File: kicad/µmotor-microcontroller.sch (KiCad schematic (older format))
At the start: 9 parts, among them J201 TX, J202 RX, J203 SWDIO, J204 SWCLK, J205 GND, U201 STM32F042F6Px

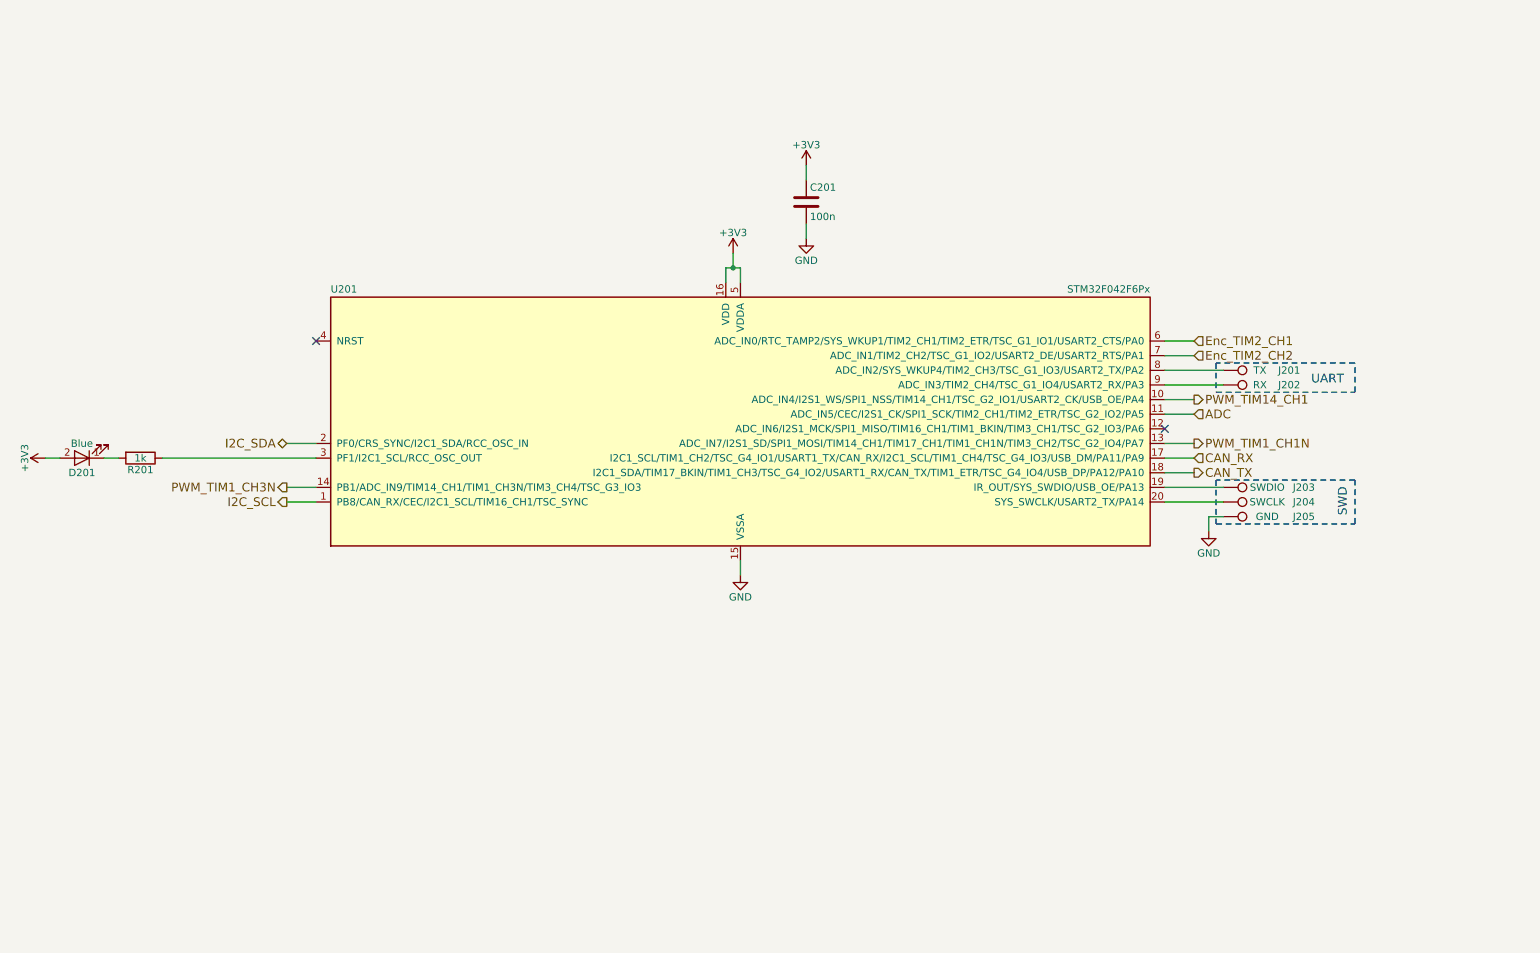
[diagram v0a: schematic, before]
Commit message: second design: STM32L432KC µC with DRV8323S gate driver and FDMD82xx FETs
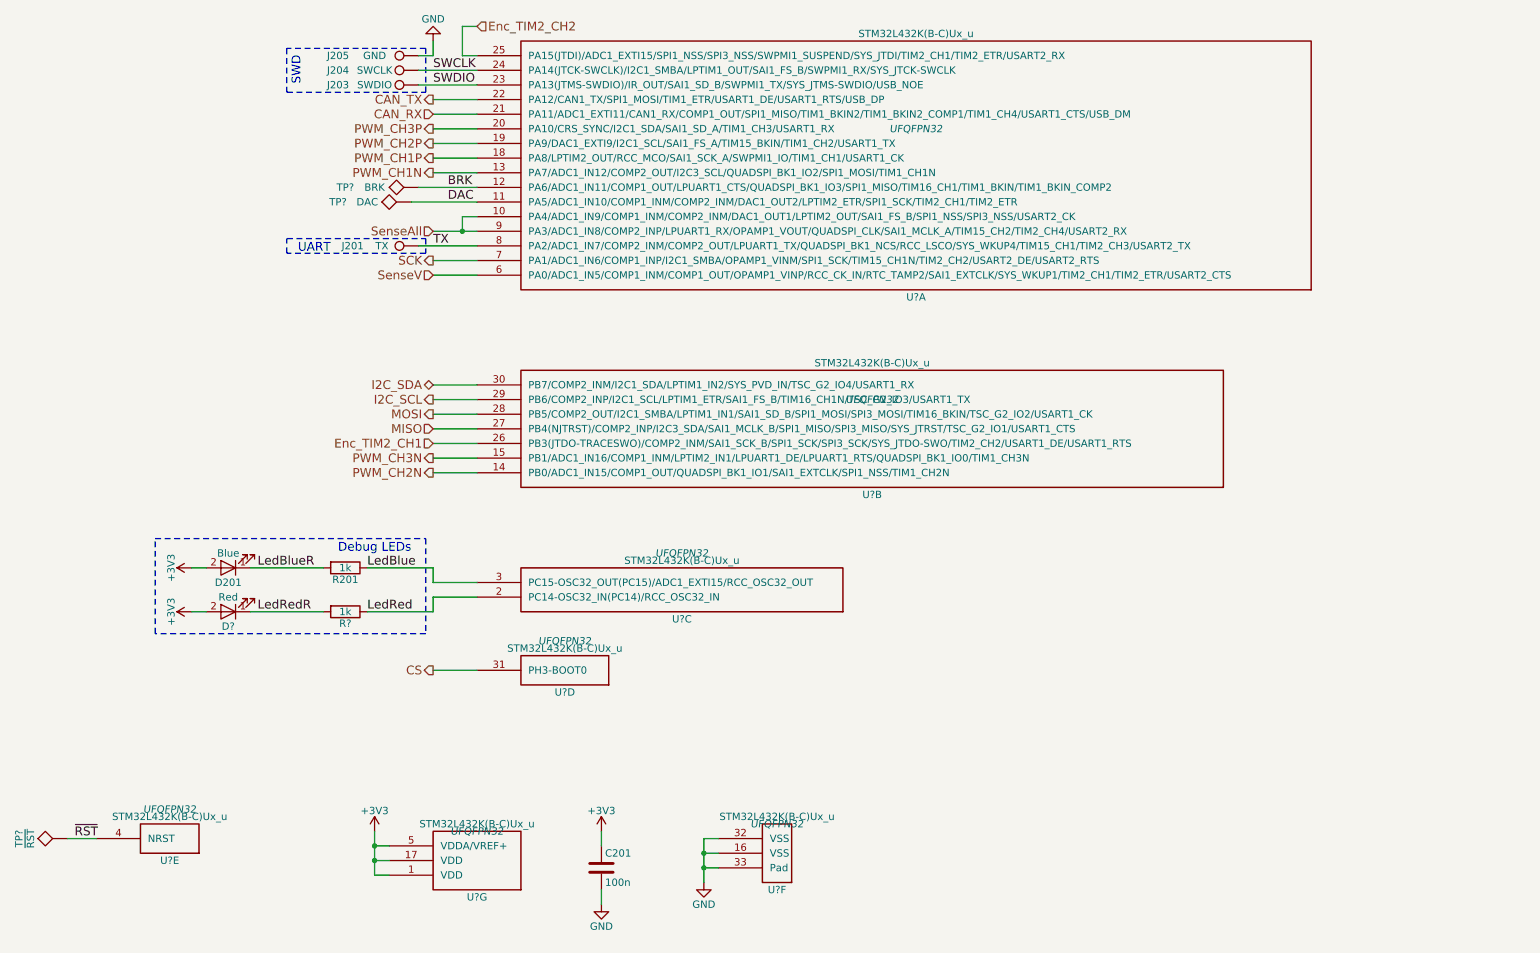
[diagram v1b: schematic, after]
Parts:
- removed J202: RX, Measurement_Points:Measurement_Point_Round-SMD-Pad_Small, symbol TEST_1P
- removed U201: STM32F042F6Px, Housings_SSOP:TSSOP-20_4.4x6.5mm_Pitch0.65mm, symbol STM32F042F6Px
- added D?: Red, LEDs:LED_0603, symbol LED
- added R?: 1k, Resistors_SMD:R_0603, symbol R
- added TP?: ~RST, symbol TEST
- added TP?: BRK, symbol TEST
- added TP?: DAC, symbol TEST
- added U? (x7): STM32L432K(B-C)Ux_u, UFQFPN32, symbol STM32L432K(B-C)Ux_u
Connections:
- net +3V3: now also D?.2 (A), U?.1 (VDD), U?.17 (VDD), U?.5 (VDDA/VREF+)
- net CAN_RX: now also U?.21 (PA11/ADC1_EXTI11/CAN1_RX/COMP1_OUT/SPI1_MISO/TIM1_BKIN2/TIM1_BKIN2_COMP1/TIM1_CH4/USART1_CTS/USB_DM)
- net CAN_TX: now also U?.22 (PA12/CAN1_TX/SPI1_MOSI/TIM1_ETR/USART1_DE/USART1_RTS/USB_DP)
- net Enc_TIM2_CH1: now also U?.26 (PB3(JTDO-TRACESWO)/COMP2_INM/SAI1_SCK_B/SPI1_SCK/SPI3_SCK/SYS_JTDO-SWO/TIM2_CH2/USART1_DE/USART1_RTS)
- net Enc_TIM2_CH2: now also U?.25 (PA15(JTDI)/ADC1_EXTI15/SPI1_NSS/SPI3_NSS/SWPMI1_SUSPEND/SYS_JTDI/TIM2_CH1/TIM2_ETR/USART2_RX)
- net GND: now also U?.16 (VSS), U?.32 (VSS), U?.33 (Pad)
- net I2C_SCL: now also U?.29 (PB6/COMP2_INP/I2C1_SCL/LPTIM1_ETR/SAI1_FS_B/TIM16_CH1N/TSC_G2_IO3/USART1_TX)
- net I2C_SDA: now also U?.30 (PB7/COMP2_INM/I2C1_SDA/LPTIM1_IN2/SYS_PVD_IN/TSC_G2_IO4/USART1_RX)
- net SWDIO: now reaches J203.1
- net SWDIO: now also U?.23 (PA13(JTMS-SWDIO)/IR_OUT/SAI1_SD_B/SWPMI1_TX/SYS_JTMS-SWDIO/USB_NOE)
- net SWCLK: now reaches J204.1
- net SWCLK: now also U?.24 (PA14(JTCK-SWCLK)/I2C1_SMBA/LPTIM1_OUT/SAI1_FS_B/SWPMI1_RX/SYS_JTCK-SWCLK)
- net LedBlue: now reaches R201.1
- net LedBlue: now also U?.3 (PC15-OSC32_OUT(PC15)/ADC1_EXTI15/RCC_OSC32_OUT)
- net TX: now reaches J201.1
- net TX: now also U?.8 (PA2/ADC1_IN7/COMP2_INM/COMP2_OUT/LPUART1_TX/QUADSPI_BK1_NCS/RCC_LSCO/SYS_WKUP4/TIM15_CH1/TIM2_CH3/USART2_TX)
- net LedBlueR: now reaches D201.1 (K), R201.2
- new net BRK: TP?.1, U?.12 (PA6/ADC1_IN11/COMP1_OUT/LPUART1_CTS/QUADSPI_BK1_IO3/SPI1_MISO/TIM16_CH1/TIM1_BKIN/TIM1_BKIN_COMP2)
- new net CS: U?.31 (PH3-BOOT0)
- new net DAC: TP?.1, U?.11 (PA5/ADC1_IN10/COMP1_INM/COMP2_INM/DAC1_OUT2/LPTIM2_ETR/SPI1_SCK/TIM2_CH1/TIM2_ETR)
- new net LedRed: R?.1, U?.2 (PC14-OSC32_IN(PC14)/RCC_OSC32_IN)
- new net LedRedR: D?.1 (K), R?.2
- new net MISO: U?.27 (PB4(NJTRST)/COMP2_INP/I2C3_SDA/SAI1_MCLK_B/SPI1_MISO/SPI3_MISO/SYS_JTRST/TSC_G2_IO1/USART1_CTS)
- new net MOSI: U?.28 (PB5/COMP2_OUT/I2C1_SMBA/LPTIM1_IN1/SAI1_SD_B/SPI1_MOSI/SPI3_MOSI/TIM16_BKIN/TSC_G2_IO2/USART1_CK)
- new net PWM_CH1N: U?.13 (PA7/ADC1_IN12/COMP2_OUT/I2C3_SCL/QUADSPI_BK1_IO2/SPI1_MOSI/TIM1_CH1N)
- new net PWM_CH1P: U?.18 (PA8/LPTIM2_OUT/RCC_MCO/SAI1_SCK_A/SWPMI1_IO/TIM1_CH1/USART1_CK)
- new net PWM_CH2N: U?.14 (PB0/ADC1_IN15/COMP1_OUT/QUADSPI_BK1_IO1/SAI1_EXTCLK/SPI1_NSS/TIM1_CH2N)
- new net PWM_CH2P: U?.19 (PA9/DAC1_EXTI9/I2C1_SCL/SAI1_FS_A/TIM15_BKIN/TIM1_CH2/USART1_TX)
- new net PWM_CH3N: U?.15 (PB1/ADC1_IN16/COMP1_INM/LPTIM2_IN1/LPUART1_DE/LPUART1_RTS/QUADSPI_BK1_IO0/TIM1_CH3N)
- new net PWM_CH3P: U?.20 (PA10/CRS_SYNC/I2C1_SDA/SAI1_SD_A/TIM1_CH3/USART1_RX)
- new net SCK: U?.7 (PA1/ADC1_IN6/COMP1_INP/I2C1_SMBA/OPAMP1_VINM/SPI1_SCK/TIM15_CH1N/TIM2_CH2/USART2_DE/USART2_RTS)
- new net SenseAll: U?.10 (PA4/ADC1_IN9/COMP1_INM/COMP2_INM/DAC1_OUT1/LPTIM2_OUT/SAI1_FS_B/SPI1_NSS/SPI3_NSS/USART2_CK), U?.9 (PA3/ADC1_IN8/COMP2_INP/LPUART1_RX/OPAMP1_VOUT/QUADSPI_CLK/SAI1_MCLK_A/TIM15_CH2/TIM2_CH4/USART2_RX)
- new net SenseV: U?.6 (PA0/ADC1_IN5/COMP1_INM/COMP1_OUT/OPAMP1_VINP/RCC_CK_IN/RTC_TAMP2/SAI1_EXTCLK/SYS_WKUP1/TIM2_CH1/TIM2_ETR/USART2_CTS)
- new net ~RST: TP?.1, U?.4 (NRST)
- no-connect marks 2 -> 0
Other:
- note added: "Debug LEDs"
- moved on the sheet: C201, D201, J201, J203, J204, J205, R201

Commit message: update µC pinout, motor driver, CubeMX, add 3V3 regulator and temperature sensor
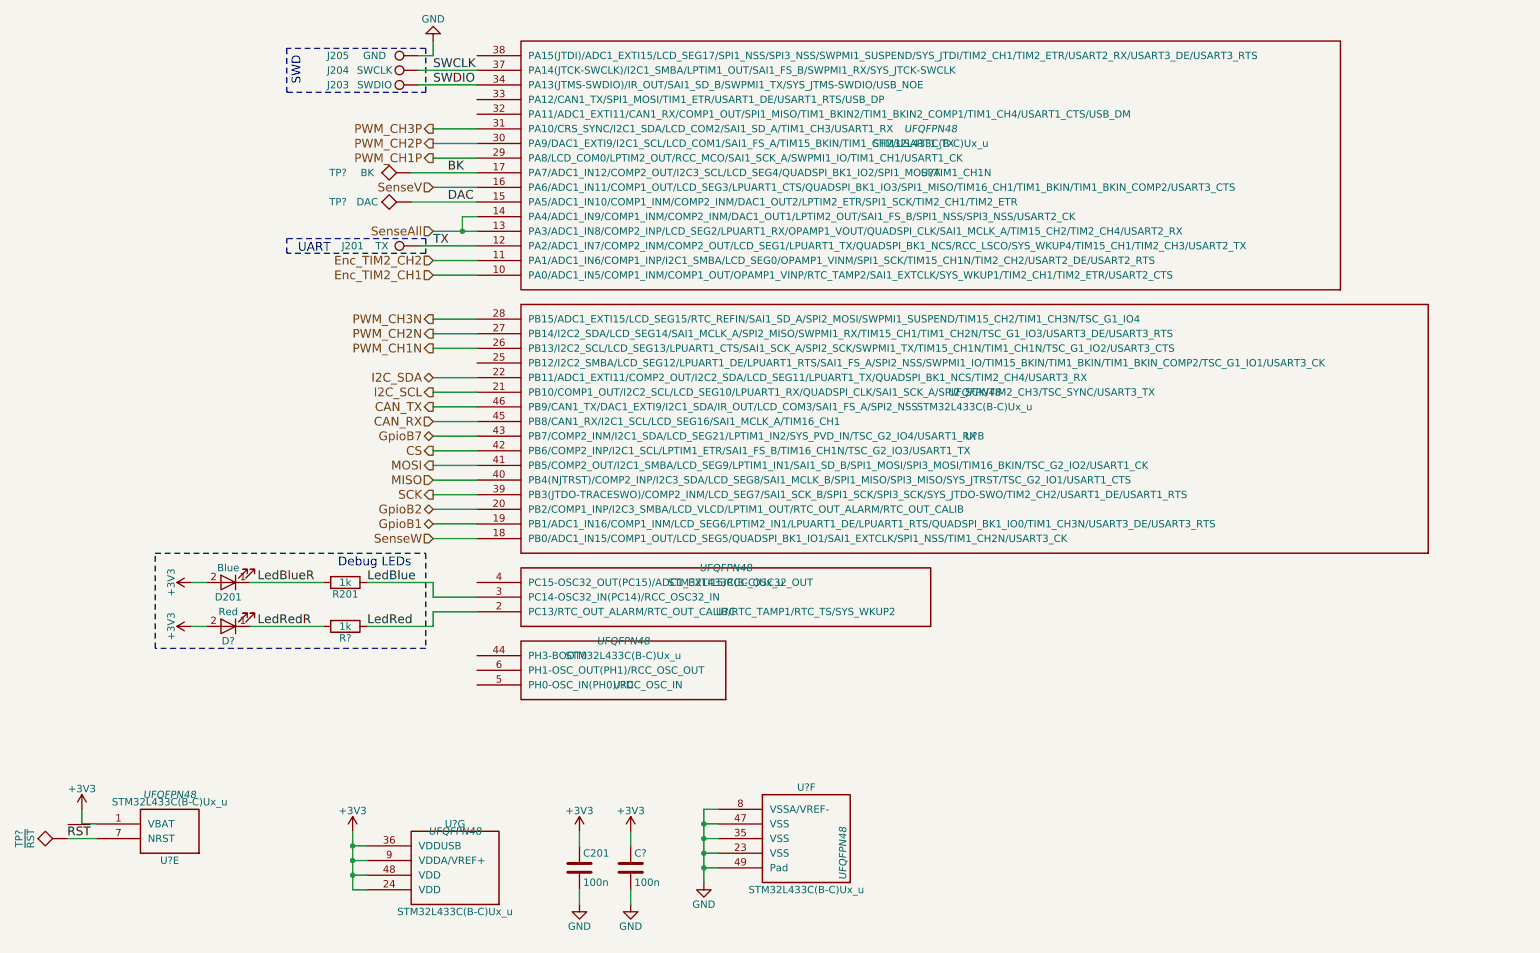
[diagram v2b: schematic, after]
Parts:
- removed TP?: BRK, symbol TEST
- removed U? (x7): STM32L432K(B-C)Ux_u, UFQFPN32, symbol STM32L432K(B-C)Ux_u
- added C?: 100n, Capacitors_SMD:C_0603, symbol C
- added TP?: BK, symbol TEST
- added U? (x7): STM32L433C(B-C)Ux_u, UFQFPN48, symbol STM32L433C(B-C)Ux_u
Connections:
- net +3V3: now also C?.1, U?.1 (VBAT), U?.24 (VDD), U?.36 (VDDUSB), U?.48 (VDD), U?.9 (VDDA/VREF+)
- net CAN_RX: now also U?.45 (PB8/CAN1_RX/I2C1_SCL/LCD_SEG16/SAI1_MCLK_A/TIM16_CH1)
- net CAN_TX: now also U?.46 (PB9/CAN1_TX/DAC1_EXTI9/I2C1_SDA/IR_OUT/LCD_COM3/SAI1_FS_A/SPI2_NSS)
- net CS: now also U?.42 (PB6/COMP2_INP/I2C1_SCL/LPTIM1_ETR/SAI1_FS_B/TIM16_CH1N/TSC_G2_IO3/USART1_TX)
- net DAC: now also U?.15 (PA5/ADC1_IN10/COMP1_INM/COMP2_INM/DAC1_OUT2/LPTIM2_ETR/SPI1_SCK/TIM2_CH1/TIM2_ETR)
- net Enc_TIM2_CH1: now also U?.10 (PA0/ADC1_IN5/COMP1_INM/COMP1_OUT/OPAMP1_VINP/RTC_TAMP2/SAI1_EXTCLK/SYS_WKUP1/TIM2_CH1/TIM2_ETR/USART2_CTS)
- net Enc_TIM2_CH2: now also U?.11 (PA1/ADC1_IN6/COMP1_INP/I2C1_SMBA/LCD_SEG0/OPAMP1_VINM/SPI1_SCK/TIM15_CH1N/TIM2_CH2/USART2_DE/USART2_RTS)
- net GND: now also C?.2, U?.23 (VSS), U?.35 (VSS), U?.47 (VSS), U?.49 (Pad), U?.8 (VSSA/VREF-)
- net I2C_SCL: now also U?.21 (PB10/COMP1_OUT/I2C2_SCL/LCD_SEG10/LPUART1_RX/QUADSPI_CLK/SAI1_SCK_A/SPI2_SCK/TIM2_CH3/TSC_SYNC/USART3_TX)
- net I2C_SDA: now also U?.22 (PB11/ADC1_EXTI11/COMP2_OUT/I2C2_SDA/LCD_SEG11/LPUART1_TX/QUADSPI_BK1_NCS/TIM2_CH4/USART3_RX)
- net LedBlue: now also U?.3 (PC14-OSC32_IN(PC14)/RCC_OSC32_IN)
- net LedRed: now also U?.2 (PC13/RTC_OUT_ALARM/RTC_OUT_CALIB/RTC_TAMP1/RTC_TS/SYS_WKUP2)
- net MISO: now also U?.40 (PB4(NJTRST)/COMP2_INP/I2C3_SDA/LCD_SEG8/SAI1_MCLK_B/SPI1_MISO/SPI3_MISO/SYS_JTRST/TSC_G2_IO1/USART1_CTS)
- net MOSI: now also U?.41 (PB5/COMP2_OUT/I2C1_SMBA/LCD_SEG9/LPTIM1_IN1/SAI1_SD_B/SPI1_MOSI/SPI3_MOSI/TIM16_BKIN/TSC_G2_IO2/USART1_CK)
- net PWM_CH1N: now also U?.26 (PB13/I2C2_SCL/LCD_SEG13/LPUART1_CTS/SAI1_SCK_A/SPI2_SCK/SWPMI1_TX/TIM15_CH1N/TIM1_CH1N/TSC_G1_IO2/USART3_CTS)
- net PWM_CH1P: now also U?.29 (PA8/LCD_COM0/LPTIM2_OUT/RCC_MCO/SAI1_SCK_A/SWPMI1_IO/TIM1_CH1/USART1_CK)
- net PWM_CH2N: now also U?.27 (PB14/I2C2_SDA/LCD_SEG14/SAI1_MCLK_A/SPI2_MISO/SWPMI1_RX/TIM15_CH1/TIM1_CH2N/TSC_G1_IO3/USART3_DE/USART3_RTS)
- net PWM_CH2P: now also U?.30 (PA9/DAC1_EXTI9/I2C1_SCL/LCD_COM1/SAI1_FS_A/TIM15_BKIN/TIM1_CH2/USART1_TX)
- net PWM_CH3N: now also U?.28 (PB15/ADC1_EXTI15/LCD_SEG15/RTC_REFIN/SAI1_SD_A/SPI2_MOSI/SWPMI1_SUSPEND/TIM15_CH2/TIM1_CH3N/TSC_G1_IO4)
- net PWM_CH3P: now also U?.31 (PA10/CRS_SYNC/I2C1_SDA/LCD_COM2/SAI1_SD_A/TIM1_CH3/USART1_RX)
- net SCK: now also U?.39 (PB3(JTDO-TRACESWO)/COMP2_INM/LCD_SEG7/SAI1_SCK_B/SPI1_SCK/SPI3_SCK/SYS_JTDO-SWO/TIM2_CH2/USART1_DE/USART1_RTS)
- net SWCLK: now also U?.37 (PA14(JTCK-SWCLK)/I2C1_SMBA/LPTIM1_OUT/SAI1_FS_B/SWPMI1_RX/SYS_JTCK-SWCLK)
- net SWDIO: now also U?.34 (PA13(JTMS-SWDIO)/IR_OUT/SAI1_SD_B/SWPMI1_TX/SYS_JTMS-SWDIO/USB_NOE)
- net SenseAll: now also U?.13 (PA3/ADC1_IN8/COMP2_INP/LCD_SEG2/LPUART1_RX/OPAMP1_VOUT/QUADSPI_CLK/SAI1_MCLK_A/TIM15_CH2/TIM2_CH4/USART2_RX), U?.14 (PA4/ADC1_IN9/COMP1_INM/COMP2_INM/DAC1_OUT1/LPTIM2_OUT/SAI1_FS_B/SPI1_NSS/SPI3_NSS/USART2_CK)
- net SenseV: now also U?.16 (PA6/ADC1_IN11/COMP1_OUT/LCD_SEG3/LPUART1_CTS/QUADSPI_BK1_IO3/SPI1_MISO/TIM16_CH1/TIM1_BKIN/TIM1_BKIN_COMP2/USART3_CTS)
- net TX: now also U?.12 (PA2/ADC1_IN7/COMP2_INM/COMP2_OUT/LCD_SEG1/LPUART1_TX/QUADSPI_BK1_NCS/RCC_LSCO/SYS_WKUP4/TIM15_CH1/TIM2_CH3/USART2_TX)
- net ~RST: now also U?.7 (NRST)
- new net BK: TP?.1, U?.17 (PA7/ADC1_IN12/COMP2_OUT/I2C3_SCL/LCD_SEG4/QUADSPI_BK1_IO2/SPI1_MOSI/TIM1_CH1N)
- new net GpioB1: U?.19 (PB1/ADC1_IN16/COMP1_INM/LCD_SEG6/LPTIM2_IN1/LPUART1_DE/LPUART1_RTS/QUADSPI_BK1_IO0/TIM1_CH3N/USART3_DE/USART3_RTS)
- new net GpioB2: U?.20 (PB2/COMP1_INP/I2C3_SMBA/LCD_VLCD/LPTIM1_OUT/RTC_OUT_ALARM/RTC_OUT_CALIB)
- new net GpioB7: U?.43 (PB7/COMP2_INM/I2C1_SDA/LCD_SEG21/LPTIM1_IN2/SYS_PVD_IN/TSC_G2_IO4/USART1_RX)
- new net SenseW: U?.18 (PB0/ADC1_IN15/COMP1_OUT/LCD_SEG5/QUADSPI_BK1_IO1/SAI1_EXTCLK/SPI1_NSS/TIM1_CH2N/USART3_CK)
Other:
- moved on the sheet: C201, D201, D?, R201, R?
